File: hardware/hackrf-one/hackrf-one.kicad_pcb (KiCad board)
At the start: 4 copper layers, 120 x 75 mm, 432 parts, among them J1 USB-MICRO-B, J10 GND_CLIP, J2 RF-SHIELD-FRAME, J3 RF-SHIELD-COVER, J4 MOUNTING_HOLE, J5 MOUNTING_HOLE, J6 MOUNTING_HOLE, J7 MOUNTING_HOLE, J8 MOUNTING_HOLE, J9 MOUNTING_HOLE, P13 GPO1, P14 XCVR_CLKOUT, P15 INTR, P16 CLKIN, P17 GPO6, P18 OEB, P19 GPO3, P2 CLKOUT, P20 GPIO, P21 REF_IN, P22 I2S, P23 DBGEN, P24 TRST, P25 LPC_ISP, P26 LPC_JTAG, P27 MIXER_SDATA, P28 SD, P29 CPLD_JTAG, P3 GND, P30 BANK2_AUX, P31 MIXER_SCLK, P32 MIXER_ENX, P33 MIXER_RESETX, P34 MIX_BYPASS, P35 !MIX_BYPASS, P37 SCL, P38 SDA, P39 SSP1_SCK, P4 ANTENNA, P40 SSP1_COPI, P41 SSP1_CIPO, P42 TX, P43 RX, P44 HP, P45 LP, P46 TX_MIX_BP, P47 RX_MIX_BP, P48 TX_AMP, P49 RX_AMP, P5 LEDS, P50 AMP_BYPASS, P51 !TX_AMP_PWR, P52 !RX_AMP_PWR, P53 CS_XCVR, P54 CS_AD, P55 TXENABLE, P56 RXENABLE, P57 XTAL2, P58 GCK1, P59 GCK2, P6 GPO4, P60 SGPIO_CLK, P61 DA0, P62 DA7, P63 DD0, P64 DD9, P65 DA4, P66 DD5, P67 RSSI, P68 SPIFI_CS, P69 VREGMODE, P7 GPO2, P70 EN_1V8, P71 ID, P72 GP_CLKIN, P73 P1_2, P74 P1_1, P75 GP_CLKIN, P76 GP_CLKIN, P77 GP_CLKIN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

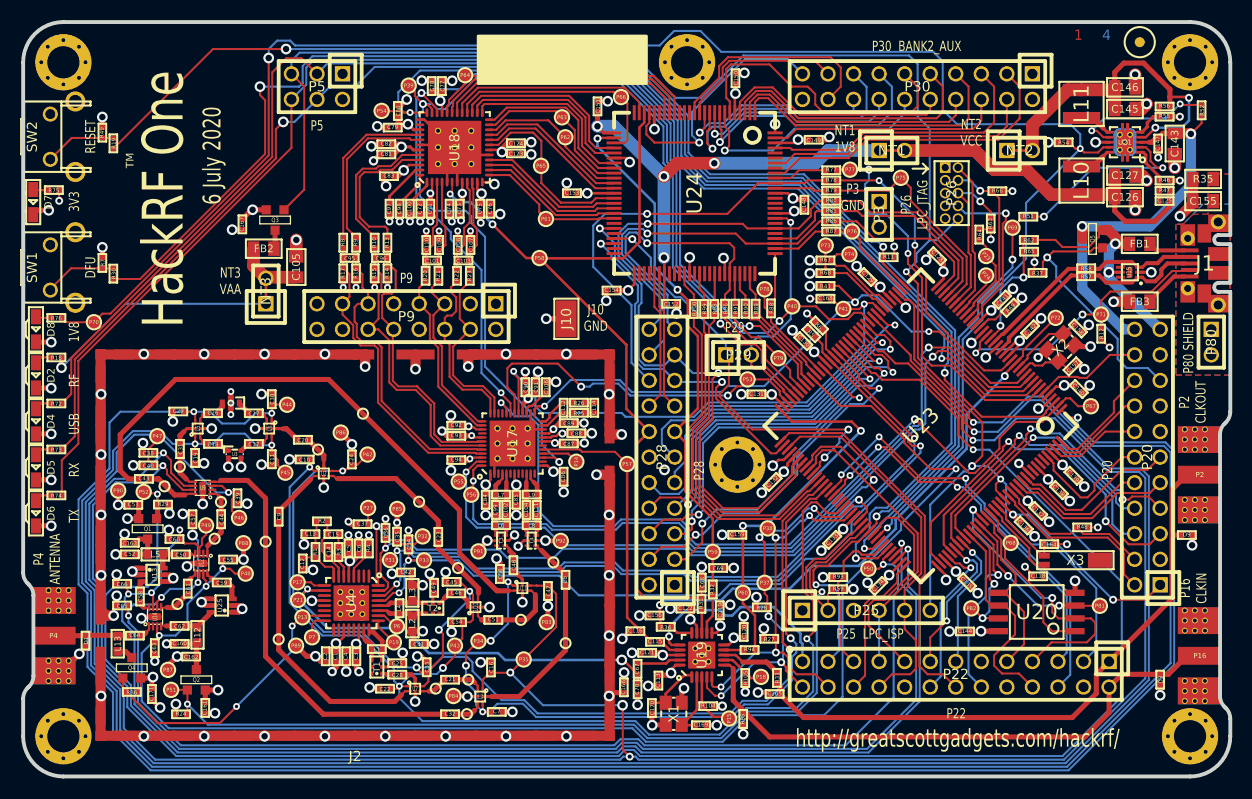
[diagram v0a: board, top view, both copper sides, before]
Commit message: HackRF One: add ADC pin straps for hardware version detection
update power supply schematic symbols
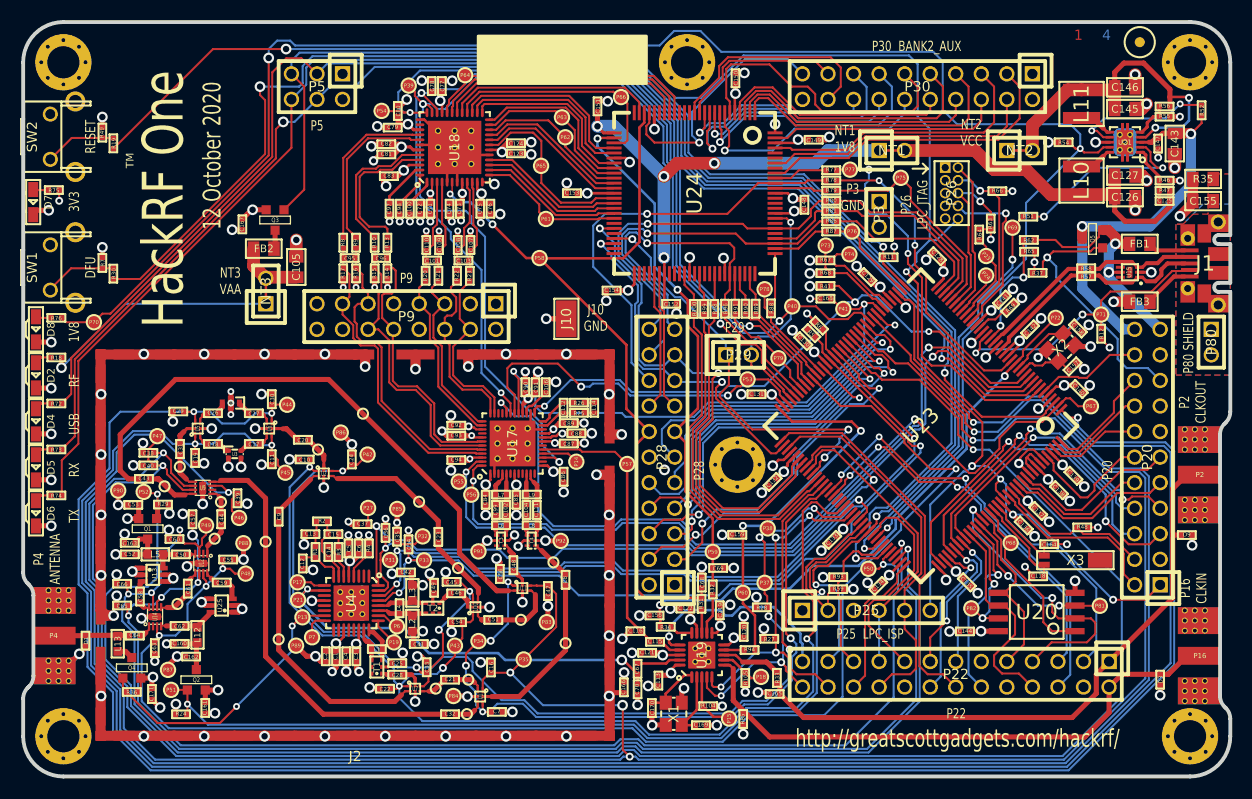
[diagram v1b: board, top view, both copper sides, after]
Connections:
- P25 pad 3: (no net) -> Net-(P25-Pad3)
- P26 pad 7: (no net) -> Net-(P26-Pad7)
- U12 pad 2: (no net) -> Net-(U12-Pad2)
- U14 pad 2: (no net) -> Net-(U14-Pad2)
- U15 pad 4: (no net) -> Net-(U15-Pad4)
- U15 pad 6: (no net) -> Net-(U15-Pad6)
- U17 pad 12: (no net) -> Net-(U17-Pad12)
- U17 pad 14: (no net) -> Net-(U17-Pad14)
- U17 pad 18: (no net) -> Net-(U17-Pad18)
- U17 pad 3: (no net) -> Net-(U17-Pad3)
- U17 pad 33: (no net) -> Net-(U17-Pad33)
- U17 pad 34: (no net) -> Net-(U17-Pad34)
- U17 pad 40: (no net) -> Net-(U17-Pad40)
- U17 pad 6: (no net) -> Net-(U17-Pad6)
- U17 pad 8: (no net) -> Net-(U17-Pad8)
- U17 pad 9: (no net) -> Net-(U17-Pad9)
- U18 pad 38: (no net) -> Net-(U18-Pad38)
- U23 pad 136: (no net) -> VCC
- U23 pad 138: (no net) -> VCC
- U23 pad 139: (no net) -> GND
- U23 pad 89: (no net) -> Net-(U23-Pad89)
- U23 pad 90: (no net) -> Net-(U23-Pad90)
- U24 pad 14: (no net) -> Net-(U24-Pad14)
- U24 pad 15: (no net) -> Net-(U24-Pad15)
- U24 pad 16: (no net) -> Net-(U24-Pad16)
- U24 pad 20: (no net) -> Net-(U24-Pad20)
- U24 pad 25: (no net) -> Net-(U24-Pad25)
- U24 pad 44: (no net) -> Net-(U24-Pad44)
- U24 pad 46: (no net) -> Net-(U24-Pad46)
- U24 pad 49: (no net) -> Net-(U24-Pad49)
- U24 pad 50: (no net) -> Net-(U24-Pad50)
- U24 pad 52: (no net) -> Net-(U24-Pad52)
- U24 pad 53: (no net) -> Net-(U24-Pad53)
- U24 pad 54: (no net) -> Net-(U24-Pad54)
- U24 pad 58: (no net) -> Net-(U24-Pad58)
- U24 pad 59: (no net) -> Net-(U24-Pad59)
- U24 pad 60: (no net) -> Net-(U24-Pad60)
- U24 pad 63: (no net) -> Net-(U24-Pad63)
- U24 pad 65: (no net) -> Net-(U24-Pad65)
- U24 pad 66: (no net) -> Net-(U24-Pad66)
- U24 pad 68: (no net) -> Net-(U24-Pad68)
- U24 pad 73: (no net) -> Net-(U24-Pad73)
- U24 pad 75: (no net) -> Net-(U24-Pad75)
- U24 pad 80: (no net) -> Net-(U24-Pad80)
- U24 pad 82: (no net) -> Net-(U24-Pad82)
- U24 pad 85: (no net) -> Net-(U24-Pad85)
- U24 pad 86: (no net) -> Net-(U24-Pad86)
- U24 pad 87: (no net) -> Net-(U24-Pad87)
- U24 pad 93: (no net) -> Net-(U24-Pad93)
- U24 pad 95: (no net) -> Net-(U24-Pad95)
- U24 pad 96: (no net) -> Net-(U24-Pad96)
- U4 pad 1: (no net) -> Net-(U4-Pad1)
- U4 pad 11: (no net) -> Net-(U4-Pad11)
- U4 pad 13: (no net) -> Net-(U4-Pad13)
- U4 pad 14: (no net) -> Net-(U4-Pad14)
- U4 pad 17: (no net) -> Net-(U4-Pad17)
- U4 pad 18: (no net) -> Net-(U4-Pad18)
- U4 pad 2: (no net) -> Net-(U4-Pad2)
- U4 pad 20: (no net) -> Net-(U4-Pad20)
- U4 pad 21: (no net) -> Net-(U4-Pad21)
- U4 pad 3: (no net) -> Net-(U4-Pad3)
- U9 pad 2: (no net) -> Net-(U9-Pad2)
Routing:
- net VCC: track 181.1 -> 185.9 mm
- net GND: track 592.3 -> 596.0 mm
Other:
- board text added: "12 October 2020"
- board text removed: "6 July 2020"

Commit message: HackRF One: update silkscreen
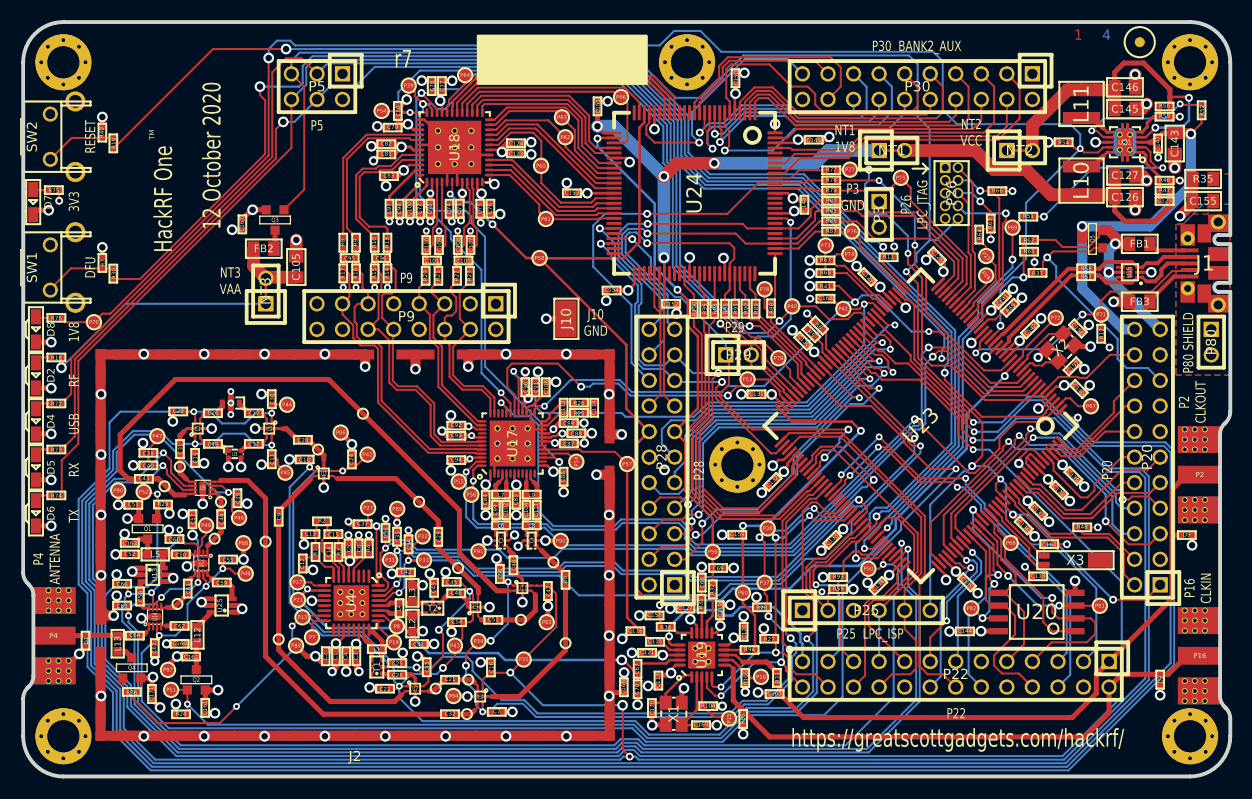
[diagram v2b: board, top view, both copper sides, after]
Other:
- board text added: "https://greatscottgadgets.com/hackrf/"
- board text added: "r7"
- board text removed: "http://greatscottgadgets.com/hackrf/"
